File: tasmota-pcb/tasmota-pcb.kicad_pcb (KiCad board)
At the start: 2 copper layers, 1 part, among them U1 ESP32_DevKit_V1_DOIT

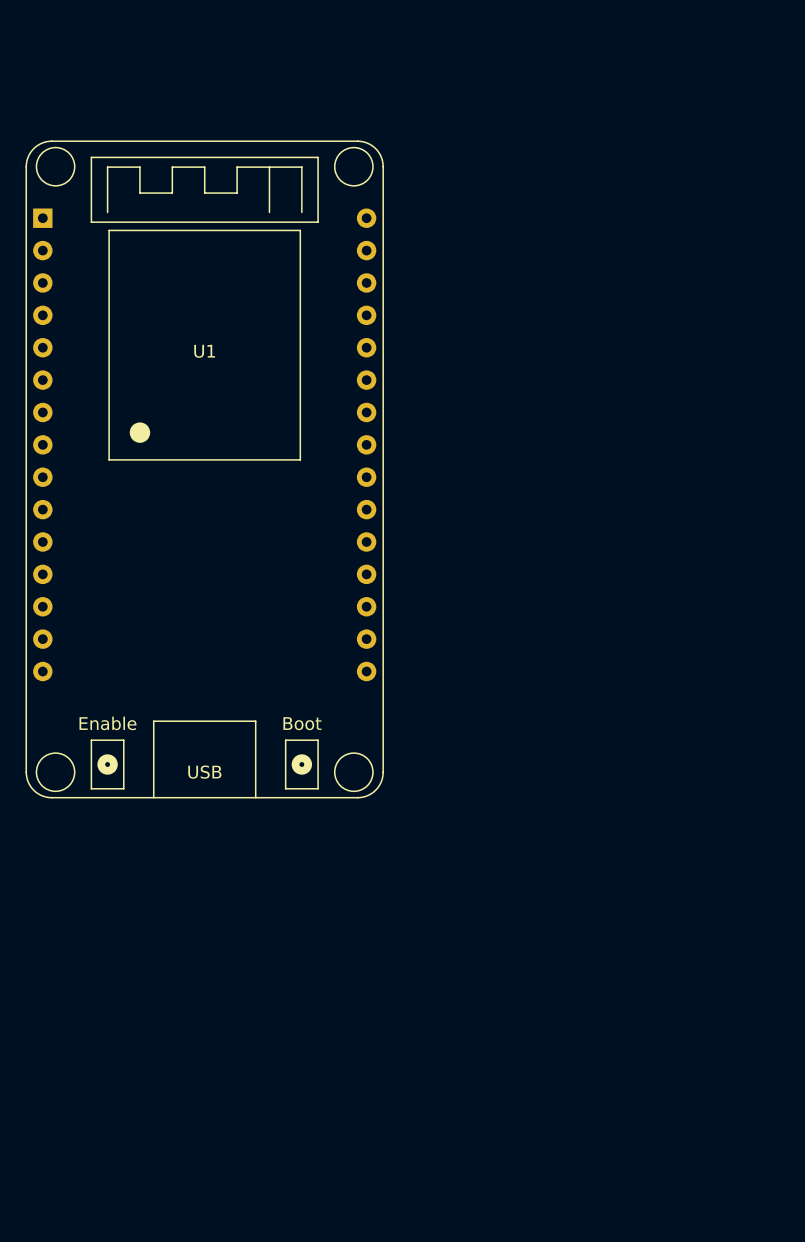
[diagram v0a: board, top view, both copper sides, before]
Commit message: Layout pcb for case
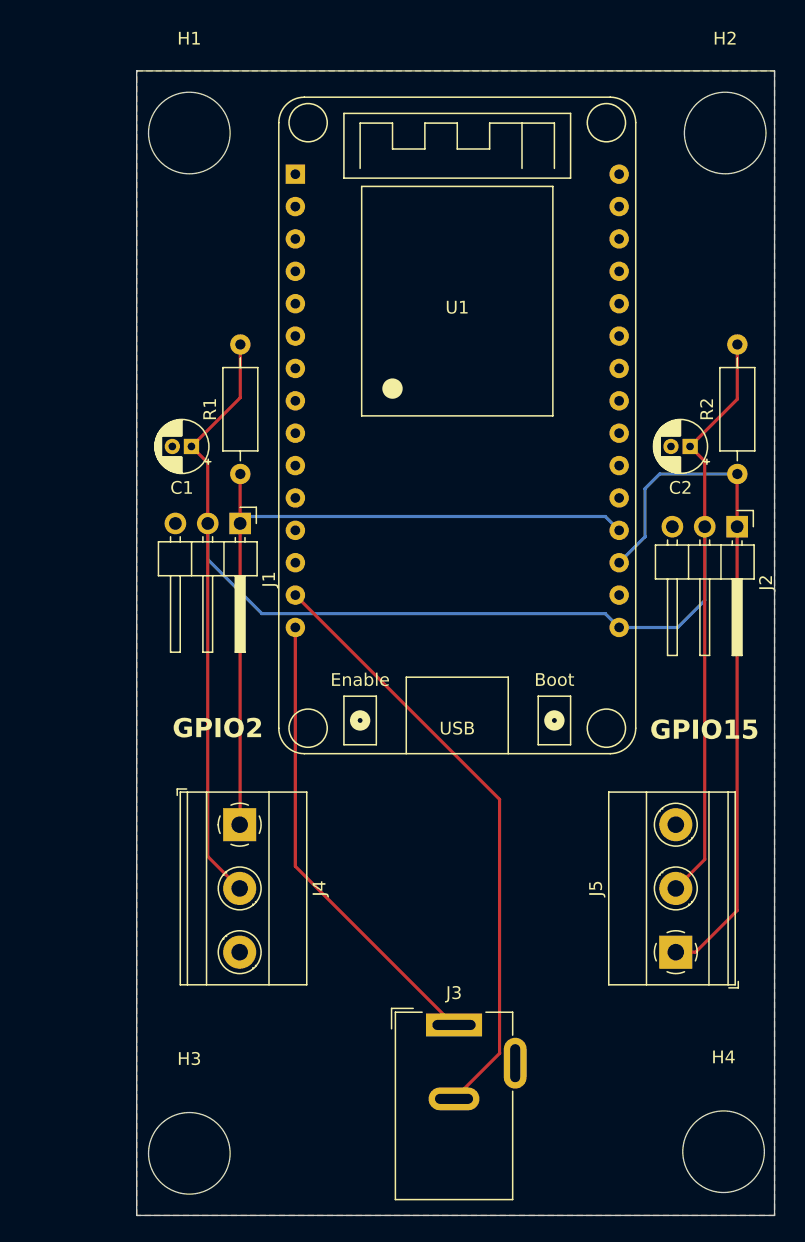
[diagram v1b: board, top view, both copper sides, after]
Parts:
- added C1: C, Capacitor_THT:CP_Radial_D4.0mm_P1.50mm, F.Cu at (132.3, 78.5)
- added C2: C, Capacitor_THT:CP_Radial_D4.0mm_P1.50mm, F.Cu at (171.4, 78.5)
- added H1: MountingHole, MountingHole:MountingHole_6.4mm_M6, F.Cu at (132.1, 53.9)
- added H2: MountingHole, MountingHole:MountingHole_6.4mm_M6, F.Cu at (174.2, 53.9)
- added H3: MountingHole, MountingHole:MountingHole_6.4mm_M6, F.Cu at (132.1, 133.9)
- added H4: MountingHole, MountingHole:MountingHole_6.4mm_M6, F.Cu at (174.1, 133.8)
- added J1: Conn_01x03, Connector_PinHeader_2.54mm:PinHeader_1x03_P2.54mm_Horizontal, F.Cu at (136.1, 84.5)
- added J2: Conn_01x03, Connector_PinHeader_2.54mm:PinHeader_1x03_P2.54mm_Horizontal, F.Cu at (175.1, 84.8)
- added J3: Barrel_Jack, Connector_BarrelJack:BarrelJack_Wuerth_6941xx301002, F.Cu at (152.9, 123.9)
- added J4: Screw_Terminal_01x03, TerminalBlock_Phoenix:TerminalBlock_Phoenix_MKDS-1,5-3_1x03_P5.00mm_Horizontal, F.Cu at (136.1, 108.2)
- added J5: Screw_Terminal_01x03, TerminalBlock_Phoenix:TerminalBlock_Phoenix_MKDS-1,5-3_1x03_P5.00mm_Horizontal, F.Cu at (170.3, 118.2)
- added R1: 4k7, Resistor_THT:R_Axial_DIN0207_L6.3mm_D2.5mm_P10.16mm_Horizontal, F.Cu at (136.1, 80.6)
- added R2: 4k7, Resistor_THT:R_Axial_DIN0207_L6.3mm_D2.5mm_P10.16mm_Horizontal, F.Cu at (175.1, 80.6)
- moved U1 20.1 mm to (153.2, 57.1)
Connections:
- U1 pad 14: unconnected-(U1-GND-Pad14) -> GND1
- U1 pad 15: unconnected-(U1-VIN-Pad15) -> VDC
- U1 pad 16: unconnected-(U1-3V3-Pad16) -> +3V3
- U1 pad 17: unconnected-(U1-GND-Pad17) -> GND
- U1 pad 18: unconnected-(U1-IO15-Pad18) -> /GPIO15
- U1 pad 19: unconnected-(U1-IO2-Pad19) -> /GPIO2
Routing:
- net +3V3: track 0.00 -> 142.1 mm
- net /GPIO2: track 0.00 -> 57.9 mm
- net /GPIO15: track 0.00 -> 55.1 mm
- net GND1: track 0.00 -> 47.6 mm
- net VDC: track 0.00 -> 36.3 mm
- added copper zone on B.Cu, net GND
- added copper zone on F.Cu, net GND
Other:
- board outline added: 50 x 89.8 mm
- board text added: "GPIO15"
- board text added: "GPIO2"
